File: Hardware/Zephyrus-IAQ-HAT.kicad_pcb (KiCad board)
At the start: 2 copper layers, 65 x 56 mm, 85 parts, among them J1 Conn_02x20_Odd_Even__Rpi, J10 A0, J11 A1, J12 A2, J13 A3, J14 A4, J15 A5, J16 I2C 5V, J17 PPS, J2 USART, J3 Jumper, J4 Fan 1, J5 Fan 2, J6 I2C 3.3V, J7 10103594-0001LF, J8 I2C 3.3V, J9 Alert, U1 EEPROM, U10 5V, U11 Buffer, U12 Buffer, U2 Fan Driver, U3 BSS138, U4 BSS138, U5 BSS138, U6 MUX, U7 ADC, U8 V-Shift, U9 DAC

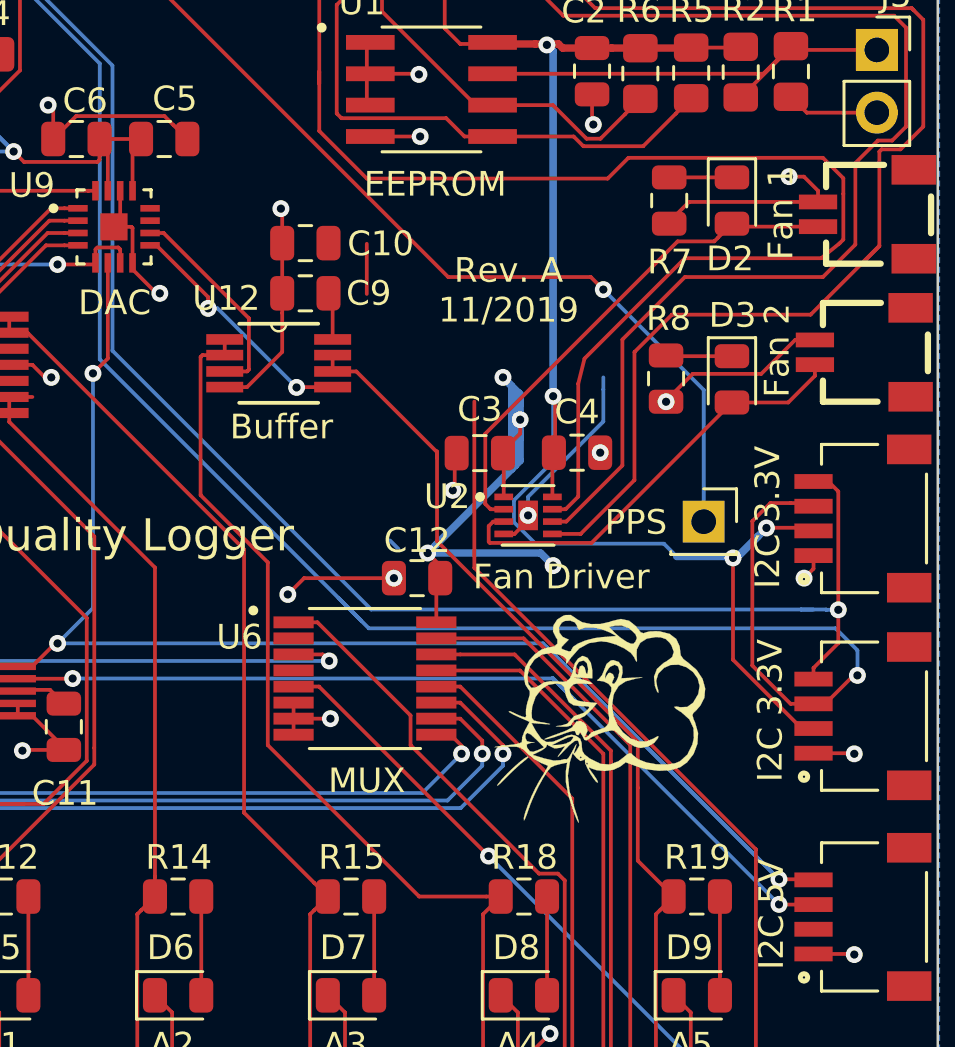
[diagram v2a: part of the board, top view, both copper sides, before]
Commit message: Update footprint for AD8532, traces, and back silkscreen.
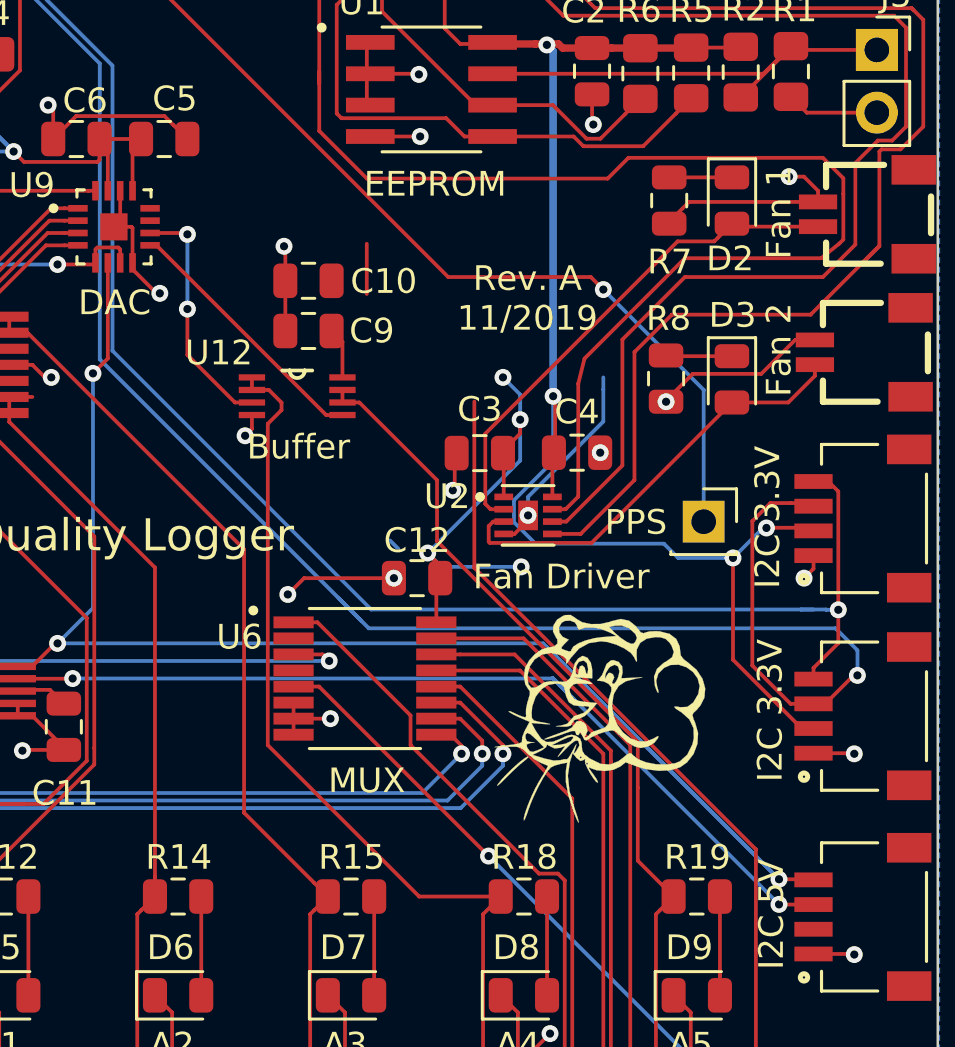
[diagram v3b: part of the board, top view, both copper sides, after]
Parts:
- removed the G*** at (232.7, 109.2)
- removed the G*** at (205.7, 109.0)
- removed the G*** at (252.2, 134.6)
- added G***: LOGO, zephyrus-iaq:crows-nest-8_3mm-6_3mm, B.Cu at (213.0, 144.5)
- added G***: LOGO, zephyrus-iaq:flying-crow-4_3mm-5_5mm, B.Cu at (209.8, 138.2)
- added G***: LOGO, zephyrus-iaq:Zephyrus-IAQ-logo-9_4mm-9_1mm, B.Cu at (211.7, 106.9)
- U12: footprint zephyrus-iaq:SOP65P490X110-8N -> zephyrus-iaq:AD8532ARMZ-MSOP8
- moved G*** 40.9 mm to (250.1, 139.3)
- moved U12 1.53 mm to (239.1, 116.6)
- moved C10 1.53 mm to (239.5, 111.9)
- moved C9 1.53 mm to (239.5, 113.9)
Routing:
- net +5V: track 166.3 -> 156.7 mm
- net GND: track 209.3 -> 205.0 mm, vias 35 -> 36
- net /Analog Port Control/BUF_OUT_4: track 39.5 -> 36.5 mm
- net /Analog Port Control/BUF_OUT_5: track 37.0 -> 35.0 mm
- net /Analog Port Control/DAC_OUT_F: track 8.52 -> 9.67 mm, vias 0 -> 2
- net +3V3: track 147.9 -> 146.9 mm
- net /Analog Port Control/DAC_OUT_E: track 10.1 -> 10.6 mm, vias 2 -> 0
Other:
- board text added: "Team Members: Aaron Jense Anthony Ciccotosto Benjamin Seal Justin Smith"
- board text removed: "Team Members: Aaron Jense Anthony Ciccotosto Justin Smith Benjamin Seal"

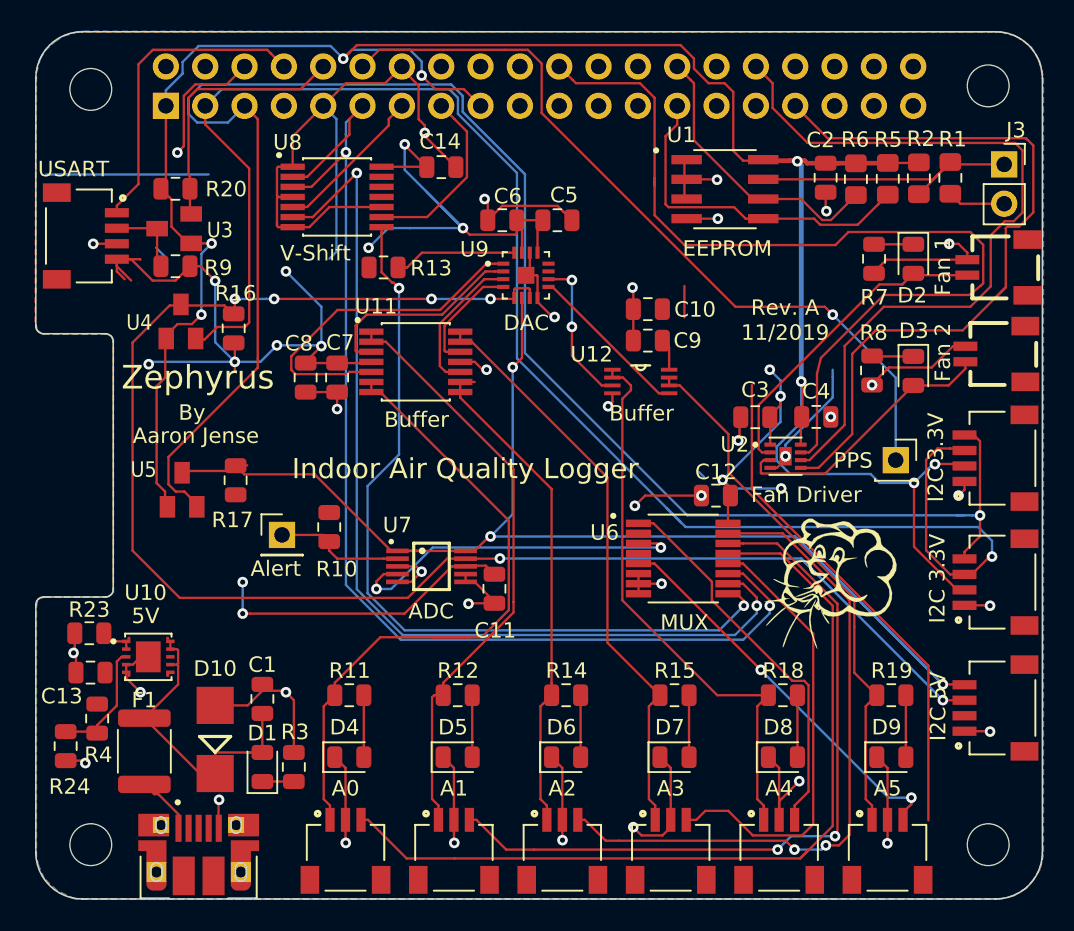
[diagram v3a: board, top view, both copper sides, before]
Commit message: Fix fan control.
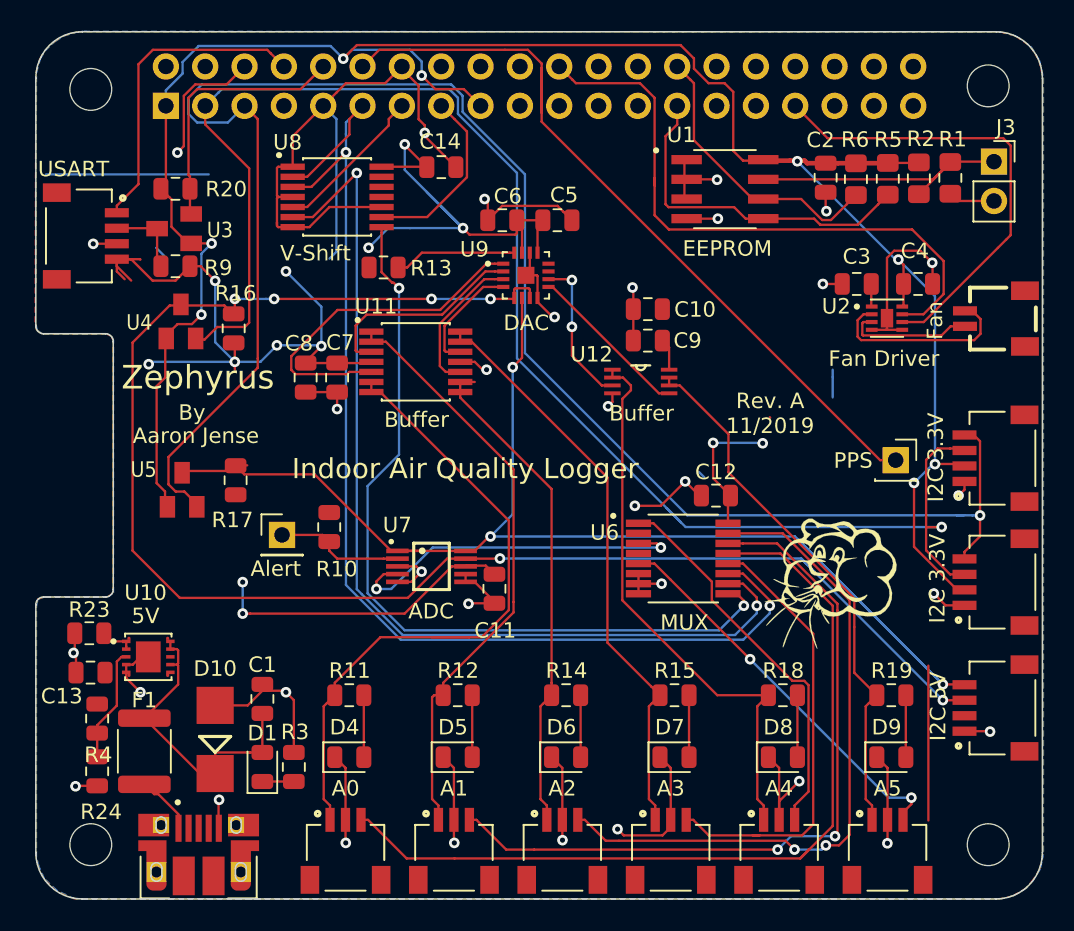
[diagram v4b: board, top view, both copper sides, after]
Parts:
- removed D2, D3: LED, Diode_SMD:D_0805_2012Metric
- removed J5: Fan 2, zephyrus-iaq:SM02B-SRSS-TB(LF)(SN)
- removed R7, R8: 330, Resistor_SMD:R_0805_2012Metric
- J4: value Fan 1 -> Fan
- moved U2 11.1 mm to (255.0, 112.5)
- moved C3 10.8 mm to (253.0, 110.3)
- moved C4 10.8 mm to (257.0, 110.3)
- moved J4 3.31 mm to (262.0, 112.5)
- moved R24 2.60 mm to (204.0, 141.8)
- moved J3 0.68 mm to (261.9, 102.4)
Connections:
- J1 pad 32: /FAN_PWM0 -> /GPIO12(PWM0)
- J4 pad 2: GND -> Net-(J4-Pad2)
- U2 pad 3: Net-(D3-Pad2) -> Net-(J4-Pad2)
- U2 pad 5: /FAN_PWM1 -> GND
- U2 pad 6: /FAN_PWM0 -> /FAN_PWM1
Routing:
- net /FAN_PWM0: track 50.3 -> 0.00 mm
- net +5V: track 156.7 -> 123.3 mm, vias 15 -> 13
- net /FAN_nSLEEP: track 59.6 -> 40.3 mm
- net /FAN_PWM1: track 49.1 -> 30.1 mm
- net Net-(D3-Pad2): track 17.8 -> 0.00 mm
- net GND: track 205.0 -> 195.7 mm, vias 36 -> 33
- net Net-(J4-Pad2): track 0.00 -> 8.27 mm
- net Net-(J4-Pad1): track 20.7 -> 12.5 mm
- net +3V3: track 146.9 -> 139.8 mm
- net /GPIO2(SDA1): track 107.4 -> 102.0 mm
- net Net-(D3-Pad1): track 2.57 -> 0.00 mm
- net Net-(D2-Pad1): track 2.54 -> 0.00 mm
- net /GPIO18(GEN1)(PWM0): track 51.1 -> 51.0 mm, vias 1 -> 0

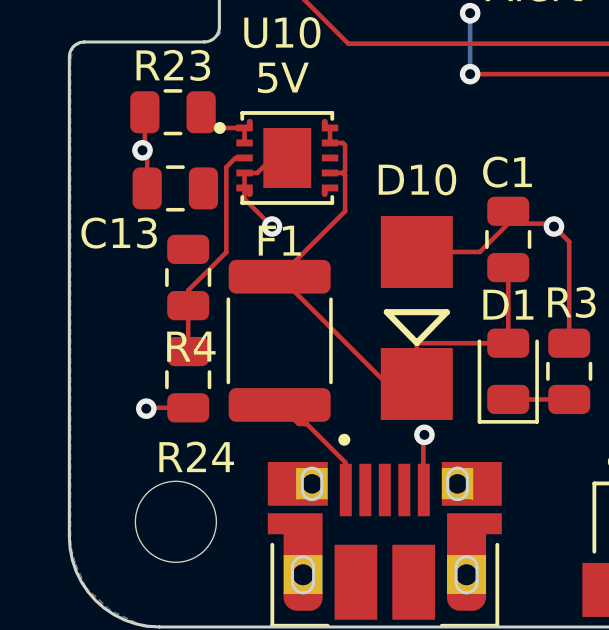
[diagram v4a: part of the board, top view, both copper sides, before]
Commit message: Add 3D footprints from SnapEDA
Hardware/Pictures are Creative Commons.
KiCad schematic symbols, 2D footprints, and 3D footprints from SnapEDA or KiCad Library.
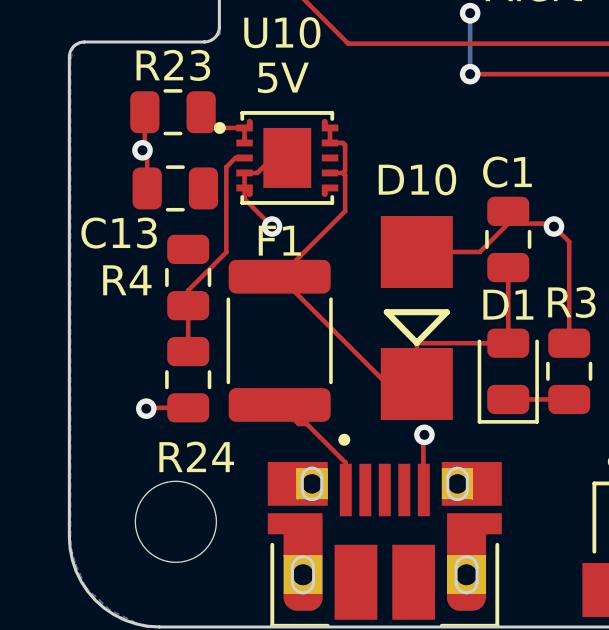
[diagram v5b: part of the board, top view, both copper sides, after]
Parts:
- D10: value SMBJ5.0A -> VAL**
- U3, U4, U5: value BSS138 -> VAL**

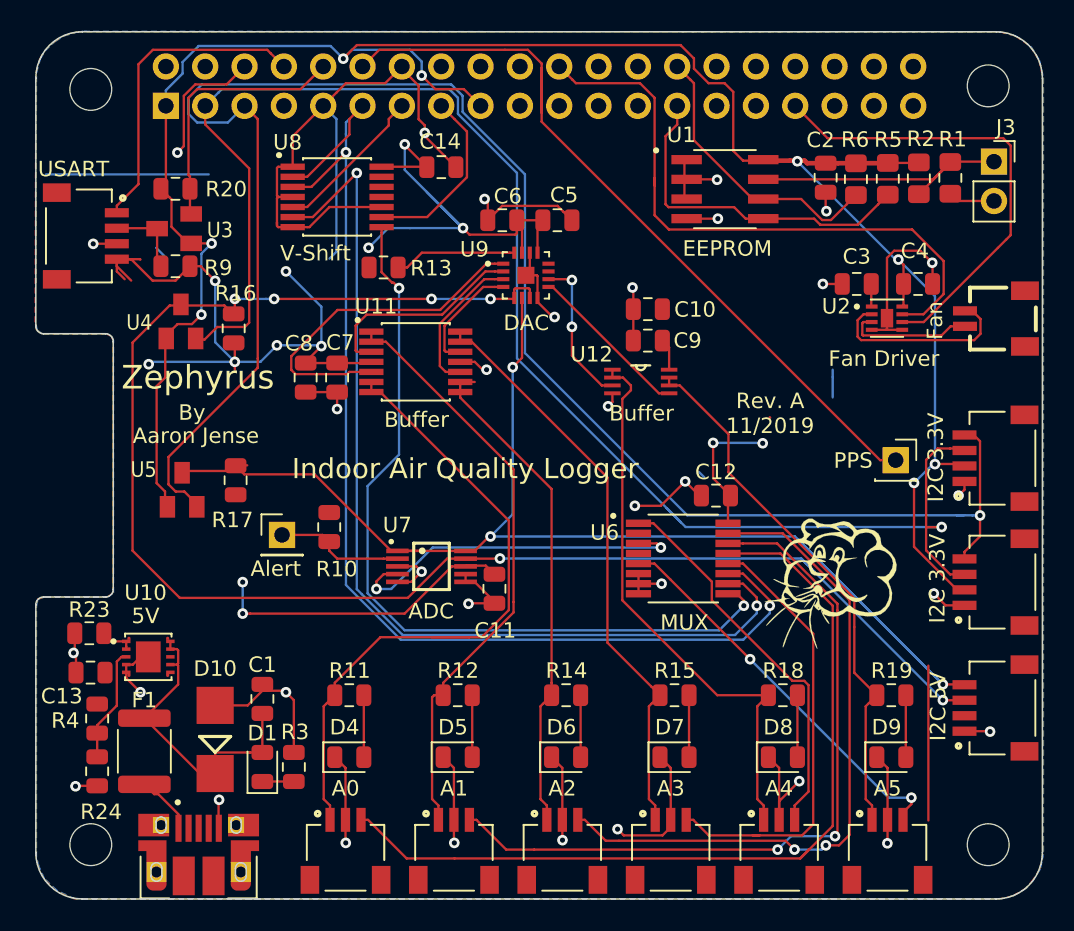
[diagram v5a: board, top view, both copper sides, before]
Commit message: AD8532ARMZ Footprint change.
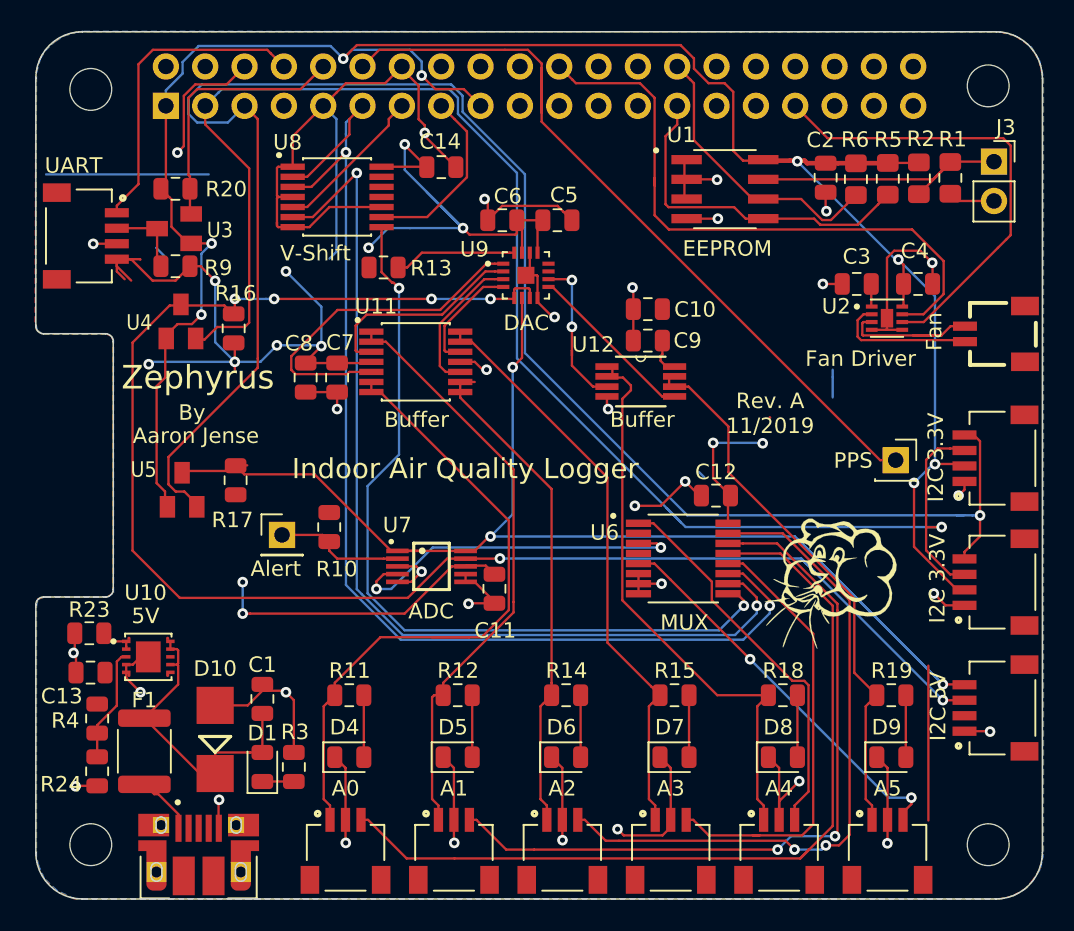
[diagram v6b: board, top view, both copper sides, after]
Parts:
- D10: value VAL** -> SMBJ5.0A
- J2: value USART -> UART
- U12: footprint zephyrus-iaq:AD8532ARMZ-MSOP8 -> zephyrus-iaq:SOP65P490X110-8N
- U3, U4, U5: value VAL** -> BSS138
- moved J4 0.99 mm to (262.0, 113.5)
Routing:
- net Net-(J4-Pad1): track 12.5 -> 9.75 mm
- net Net-(J4-Pad2): track 8.27 -> 10.1 mm
- net /Analog Port Control/DAC_OUT_F: track 9.67 -> 10.7 mm
- net /Analog Port Control/BUF_OUT_5: track 35.0 -> 35.6 mm
